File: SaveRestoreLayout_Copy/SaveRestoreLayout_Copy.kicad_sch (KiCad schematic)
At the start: 1 part

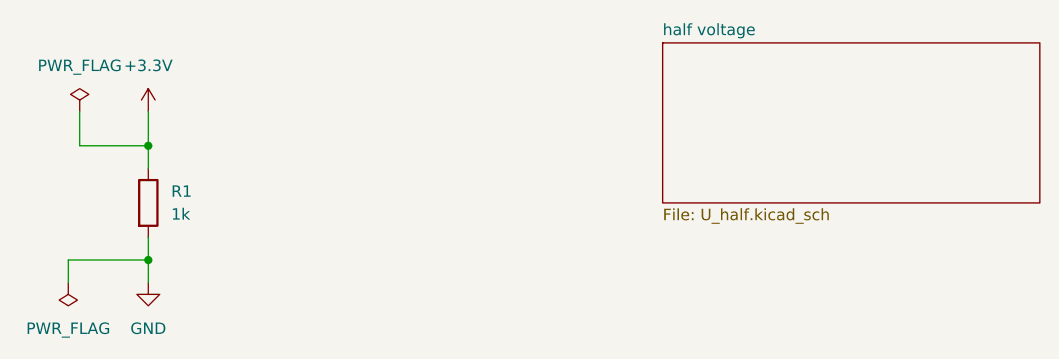
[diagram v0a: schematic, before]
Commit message: restore the layour from original
bug: the bottom layout is not restored and no via is placed
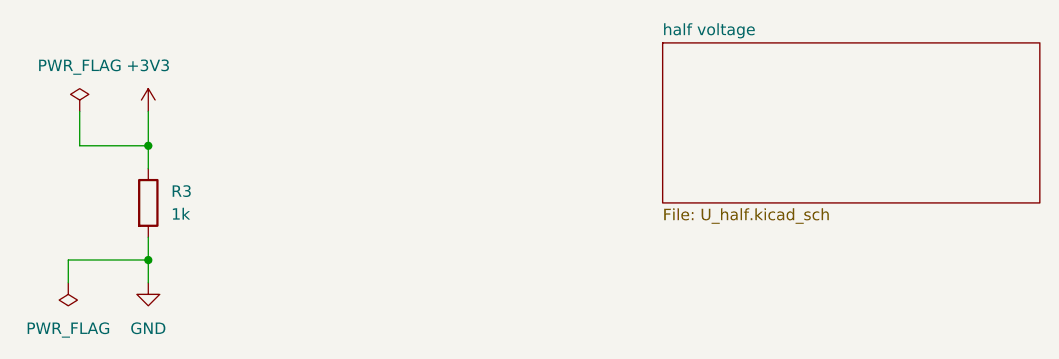
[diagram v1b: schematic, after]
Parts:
- renumbered R1 to R3
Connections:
- net +3.3V renamed +3V3
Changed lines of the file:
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@@
-    )
-  )
-  (symbol (lib_id "power:+3.3V") (at 72.39 78.74 0) (unit 1)
-    (in_bom yes) (on_board yes) (dnp no) (fields_autoplaced)
-    (property "Reference" "#PWR01" (at 72.39 82.55 0)
-      (effects (font (size 1.27 1.27)) hide)
-    )
-    (property "Value" "+3.3V" (at 72.39 73.66 0)
-      (effects (font (size 1.27 1.27)))
-    )
-    (property "Footprint" "" (at 72.39 78.74 0)
-      (effects (font (size 1.27 1.27)) hide)
-    )
-    (property "Datasheet" "" (at 72.39 78.74 0)
-      (effects (font (size 1.27 1.27)) hide)
-    )
-    (pin "1")
-    (instances
-      (project "SaveRestoreLayout_Copy"
-        (path "/f7049a7e-2ee3-423f-8203-c90463fac327"
-          (reference "#PWR01") (unit 1)
-        )
-      )
     )
   )
   (symbol (lib_id "Device:R") (at 72.39 88.9 0) (unit 1)
     (in_bom yes) (on_board yes) (dnp no) (fields_autoplaced)
-    (property "Reference" "R1" (at 74.93 87.63 0)
+    (property "Reference" "R3" (at 74.93 87.63 0)
       (effects (font (size 1.27 1.27)) (justify left))
     )
@@
       (project "SaveRestoreLayout_Copy"
         (path "/f7049a7e-2ee3-423f-8203-c90463fac327"
-          (reference "R1") (unit 1)
+          (reference "R3") (unit 1)
         )
       )
+    )
+  )
+  (symbol (lib_id "power:+3V3") (at 72.39 78.74 0) (unit 1)
+    (in_bom yes) (on_board yes) (dnp no) (fields_autoplaced)
+    (property "Reference" "#PWR05" (at 72.39 82.55 0)
+      (effects (font (size 1.27 1.27)) hide)
+    )
+    (property "Value" "+3V3" (at 72.39 73.66 0)
+      (effects (font (size 1.27 1.27)))
+    )
+    (property "Footprint" "" (at 72.39 78.74 0)
+      (effects (font (size 1.27 1.27)) hide)
+    )
+    (property "Datasheet" "" (at 72.39 78.74 0)
+      (effects (font (size 1.27 1.27)) hide)
+    )
+    (pin "1")
+    (instances
+      (project "SaveRestoreLayout_Copy"
+        (path "/f7049a7e-2ee3-423f-8203-c90463fac327"
+          (reference "#PWR05") (unit 1)
+        )
+      )
